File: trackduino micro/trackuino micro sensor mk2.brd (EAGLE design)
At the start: 43.3 x 19 mm, 42 parts, among them IC2 74AHC1G125DBV, SW1 SPST_TACT-KMR2, U1 ATMEGA168MLF, Y1 16MHZ

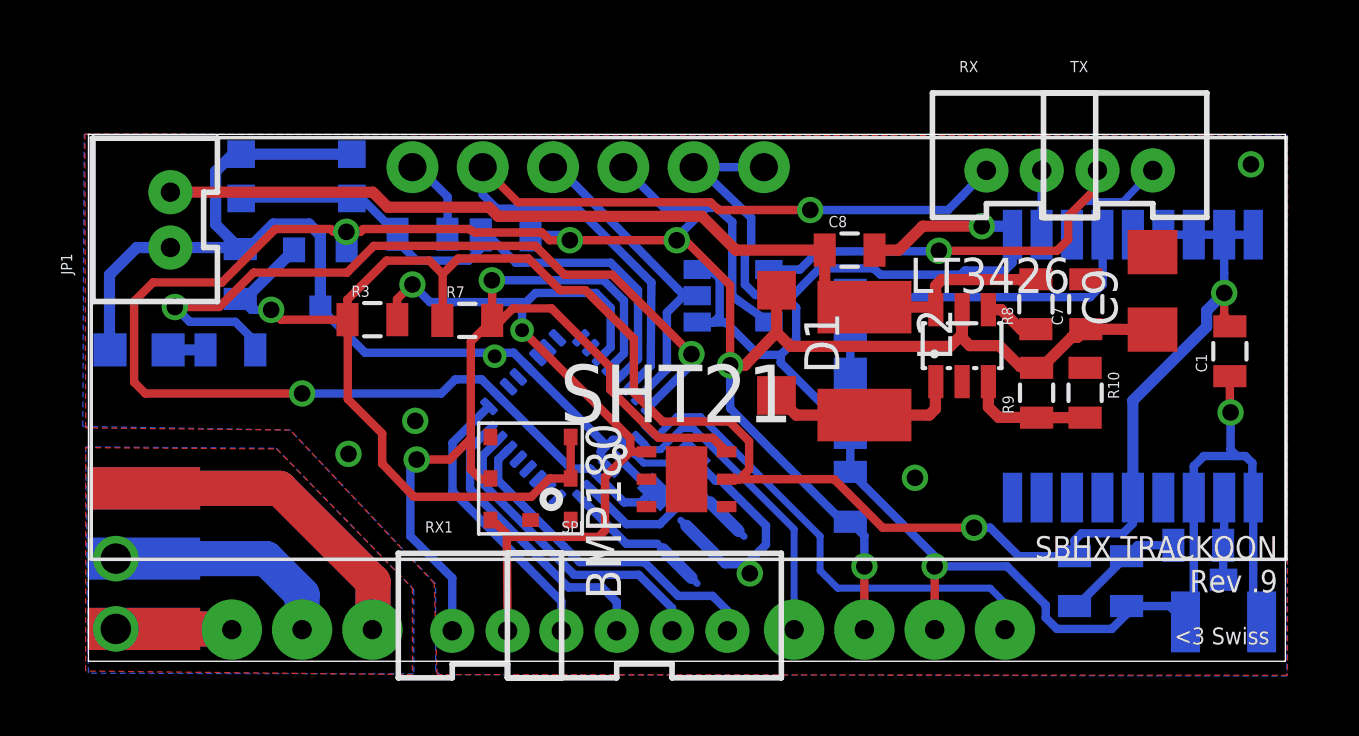
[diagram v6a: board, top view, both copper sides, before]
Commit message: Simplified Ground Polygons
simplified ground polygons and further DRC error resolutions.
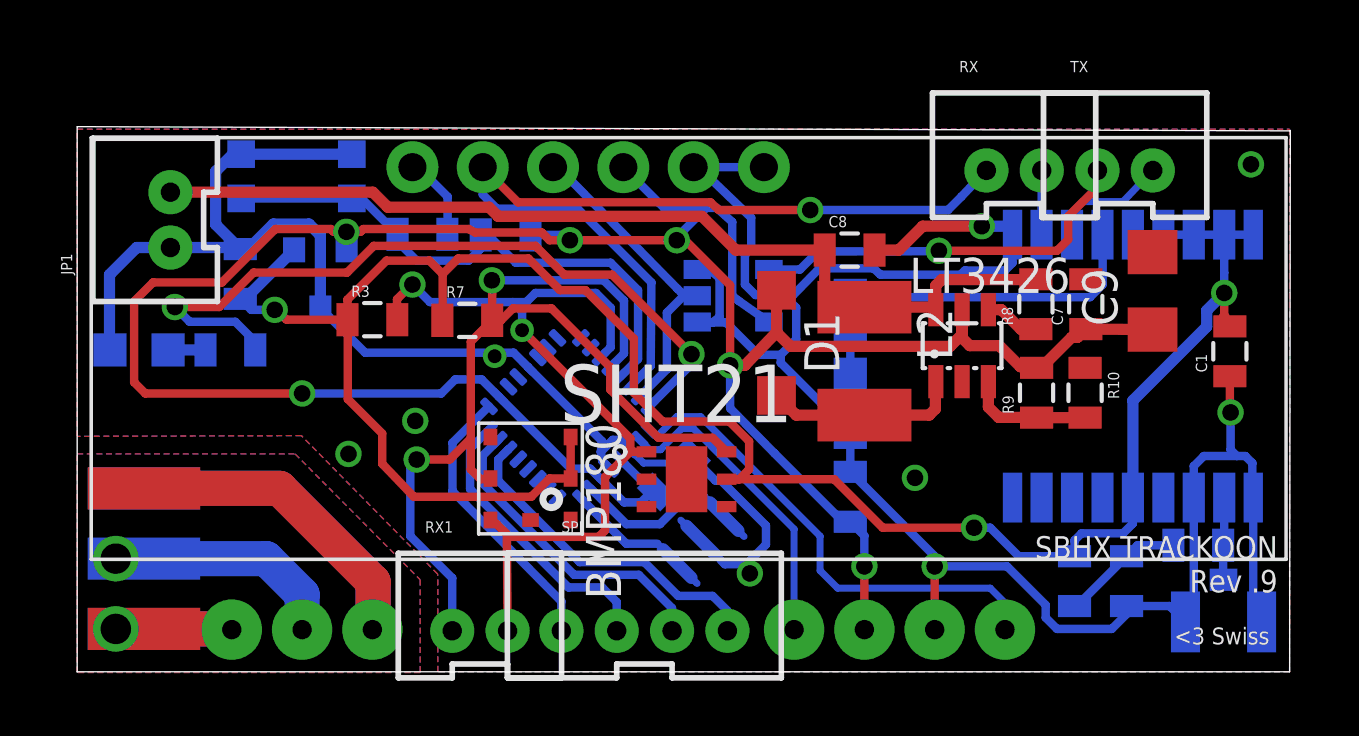
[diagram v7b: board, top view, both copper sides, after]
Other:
- board size 43.3 x 19 mm -> 43.8 x 19.7 mm
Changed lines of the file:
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@@
 <board>
 <plain>
-<wire x1="0" y1="0" x2="43.2564" y2="0" width="0" layer="20"/>
-<wire x1="43.2564" y1="0" x2="43.2564" y2="19.04" width="0" layer="20"/>
-<wire x1="43.2564" y1="19.04" x2="0" y2="19.04" width="0" layer="20"/>
-<wire x1="0" y1="19.04" x2="0" y2="0" width="0" layer="20"/>
+<wire x1="-0.4064" y1="-0.381" x2="43.4088" y2="-0.381" width="0" layer="20"/>
+<wire x1="43.4088" y1="-0.381" x2="43.4342" y2="19.167" width="0" layer="20"/>
+<wire x1="43.4342" y1="19.167" x2="-0.4064" y2="19.3194" width="0" layer="20"/>
+<wire x1="-0.4064" y1="19.3194" x2="-0.4064" y2="-0.381" width="0" layer="20"/>
 <text x="42.9768" y="4.5212" size="0.8128" layer="25" rot="R180">SBHX TRACKOON
 Rev .9</text>
@@
 <contactref element="U1" pad="5"/>
 <contactref element="FTDI" pad="6"/>
-<polygon width="0.4064" layer="1">
-<vertex x="-0.127" y="19.05"/>
-<vertex x="43.3324" y="18.9738"/>
-<vertex x="43.3324" y="-0.508"/>
-<vertex x="12.5984" y="-0.4826"/>
-<vertex x="12.4968" y="2.8194"/>
-<vertex x="7.2898" y="8.3566"/>
-<vertex x="-0.1016" y="8.4328"/>
-</polygon>
-<polygon width="0.4064" layer="16">
-<vertex x="-0.1524" y="19.05"/>
-<vertex x="43.3324" y="18.9992"/>
-<vertex x="43.307" y="-0.5334"/>
-<vertex x="12.7" y="-0.4826"/>
-<vertex x="12.5476" y="-0.3302"/>
-<vertex x="12.5476" y="2.794"/>
-<vertex x="7.2898" y="8.3566"/>
-<vertex x="-0.2032" y="8.4836"/>
-</polygon>
-<polygon width="0.4064" layer="1" orphans="yes">
-<vertex x="-0.1016" y="7.7216"/>
-<vertex x="6.8072" y="7.6708"/>
-<vertex x="11.7094" y="2.6416"/>
-<vertex x="11.7094" y="-0.4826"/>
-<vertex x="-0.1016" y="-0.3556"/>
-</polygon>
-<polygon width="0.3048" layer="16" orphans="yes">
-<vertex x="-0.1016" y="7.747"/>
-<vertex x="6.7818" y="7.6962"/>
-<vertex x="11.7602" y="2.5908"/>
-<vertex x="11.7602" y="-0.4572"/>
-<vertex x="0" y="-0.4318"/>
-</polygon>
 <contactref element="U1" pad="21"/>
 <contactref element="PTT" pad="C"/>
@@
 <wire x1="21.2344" y1="7.1628" x2="21.46439375" y2="7.39279375" width="0.254" layer="16"/>
 <wire x1="21.46439375" y1="7.39279375" x2="21.794596875" y2="7.39279375" width="0.254" layer="16"/>
+<polygon width="0.4064" layer="16">
+<vertex x="-0.4064" y="7.493"/>
+<vertex x="7.4676" y="7.493"/>
+<vertex x="11.9888" y="2.9464"/>
+<vertex x="11.9888" y="-0.4064"/>
+<vertex x="-0.4064" y="-0.4064"/>
+</polygon>
+<polygon width="0.4064" layer="1">
+<vertex x="-0.4064" y="7.493"/>
+<vertex x="7.4676" y="7.493"/>
+<vertex x="11.9888" y="2.9464"/>
+<vertex x="11.9888" y="-0.4064"/>
+<vertex x="-0.4064" y="-0.4064"/>
+</polygon>
+<polygon width="0.4064" layer="1">
+<vertex x="-0.4064" y="19.2278"/>
+<vertex x="43.4086" y="19.2278"/>
+<vertex x="43.4086" y="-0.381"/>
+<vertex x="12.6238" y="-0.381"/>
+<vertex x="12.6238" y="3.1496"/>
+<vertex x="7.6962" y="8.1534"/>
+<vertex x="-0.4064" y="8.128"/>
+</polygon>
+<polygon width="0.4064" layer="16">
+<vertex x="-0.4064" y="19.2278"/>
+<vertex x="43.4086" y="19.2278"/>
+<vertex x="43.4086" y="-0.381"/>
+<vertex x="12.6238" y="-0.381"/>
+<vertex x="12.6238" y="3.1496"/>
+<vertex x="7.6962" y="8.1534"/>
+<vertex x="-0.4064" y="8.128"/>
+</polygon>
 <wire x1="5.1816" y1="1.143" x2="5.207" y2="1.1684" width="0" layer="19" extent="1-1"/>
 <wire x1="9.398" y1="7.493" x2="6.9088" y2="6.2484" width="0" layer="19" extent="1-1"/>
@@
 <wire x1="35.8902" y1="4.6228" x2="35.6362" y2="4.3688" width="0.3048" layer="16"/>
 <wire x1="35.6362" y1="4.3688" x2="35.6362" y2="3.7956" width="0.3048" layer="16"/>
-<wire x1="9.3616" y1="12.3444" x2="6.9596" y2="12.3444" width="0.3048" layer="1"/>
-<wire x1="6.9596" y1="12.3444" x2="6.604" y2="12.7" width="0.3048" layer="1"/>
-<via x="6.604" y="12.7" extent="1-16" drill="0.6"/>
-<wire x1="6.604" y1="12.7" x2="5.8818" y2="12.7" width="0.3048" layer="16"/>
+<wire x1="9.3616" y1="12.3444" x2="7.1628" y2="12.3444" width="0.3048" layer="1"/>
+<wire x1="7.1628" y1="12.3444" x2="6.731" y2="12.7" width="0.3048" layer="1"/>
+<via x="6.731" y="12.7" extent="1-16" drill="0.6"/>
+<wire x1="6.731" y1="12.7" x2="5.8818" y2="12.7" width="0.3048" layer="16"/>
 <wire x1="5.8818" y1="12.7" x2="5.4864" y2="13.0954" width="0.3048" layer="16"/>
 <wire x1="9.3616" y1="12.3444" x2="9.3616" y2="13.07" width="0.3048" layer="1"/>
